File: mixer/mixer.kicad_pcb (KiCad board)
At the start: 2 copper layers, 20 parts, among them J1 in0, J2 in1, J3 in2, J4 out, J5 Conn_01x02, U1 OPA2134, U2 TLE2426xD

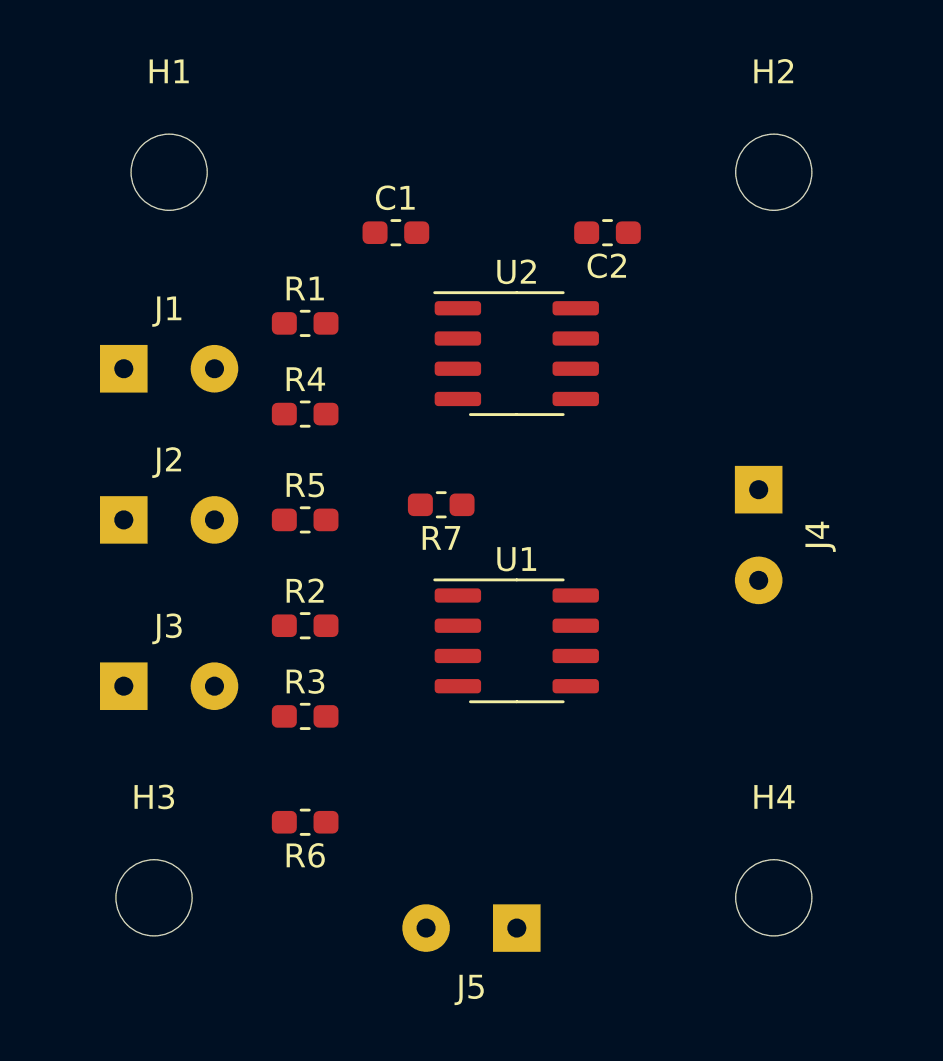
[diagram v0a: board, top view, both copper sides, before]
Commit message: Better placement
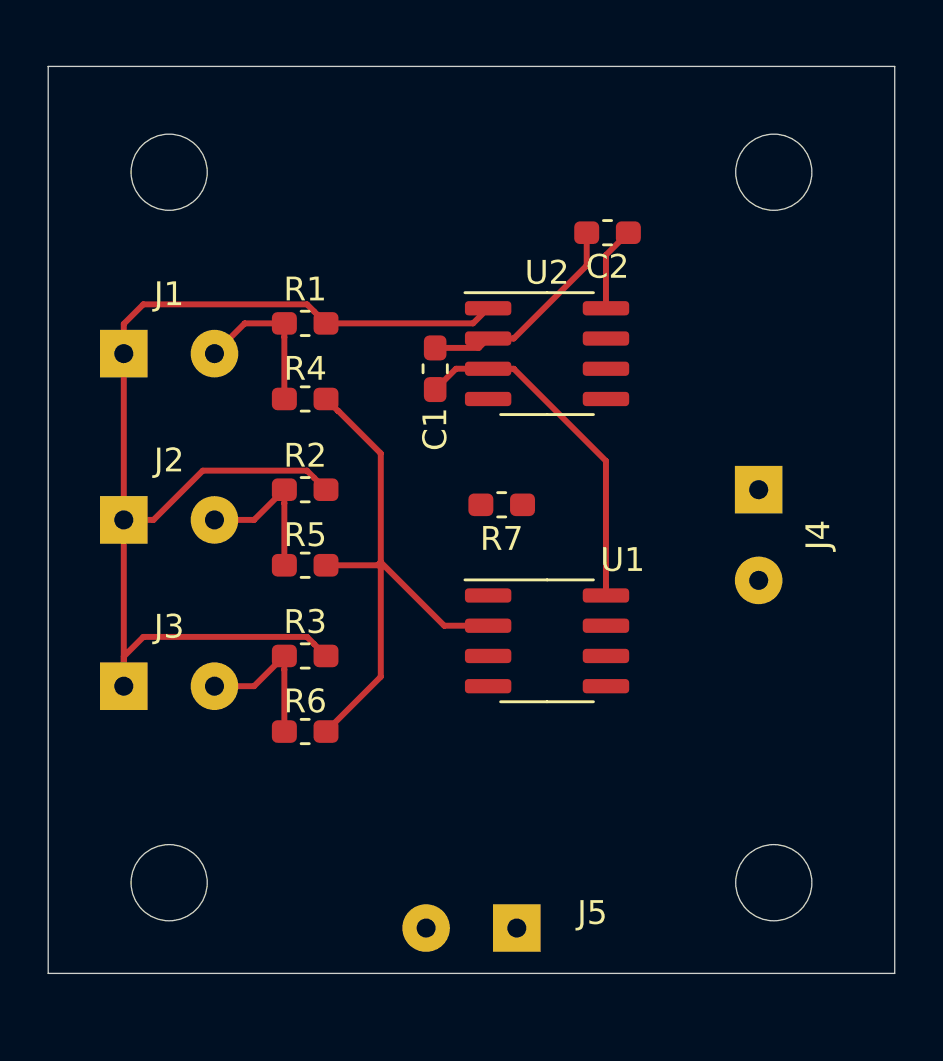
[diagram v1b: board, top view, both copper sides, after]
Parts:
- moved C1 5.95 mm to (148.3, 73.7), turned to 270 degrees
- moved R2 5.72 mm to (142.9, 78.7)
- moved R6 3.81 mm to (142.9, 88.9)
- moved R3 2.54 mm to (142.9, 85.7)
- moved R7 2.54 mm to (151.1, 79.4)
- moved R5 1.91 mm to (142.9, 81.9), turned to 180 degrees
- moved U1 1.27 mm to (153.0, 85.1)
- moved U2 1.27 mm to (153.0, 73.0)
- moved H3 0.90 mm to (137.2, 95.2)
- moved H4 0.64 mm to (162.6, 95.2)
- moved J1 0.63 mm to (135.3, 73.0)
- moved R4 0.63 mm to (142.9, 74.9), turned to 180 degrees
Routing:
- net GNDA: track 0.00 -> 51.6 mm
- net Net-(R4-Pad1): track 0.00 -> 23.9 mm
- net +9V: track 0.00 -> 14.8 mm
- net GND: track 0.00 -> 9.18 mm
- net Net-(J3-Pad2): track 0.00 -> 6.64 mm
- net Net-(J2-Pad2): track 0.00 -> 6.64 mm
- net Net-(J1-Pad2): track 0.00 -> 6.64 mm
- net Net-(C2-Pad1): track 0.00 -> 3.56 mm
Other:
- board outline added: 35.6 x 38.1 mm

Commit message: Routed
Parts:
- moved R7 0.92 mm to (150.9, 80.3)
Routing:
- net GND: track 9.18 -> 77.4 mm
- net +9V: track 14.8 -> 50.0 mm
- net GNDA: track 51.6 -> 84.9 mm
- net Net-(J4-Pad1): track 0.00 -> 16.0 mm
- net Net-(R4-Pad1): track 23.9 -> 29.3 mm
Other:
- board text added: "mixer v1"
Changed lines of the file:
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@@
   (general
     (thickness 1.6)
-    (drawings 4)
-    (tracks 54)
+    (drawings 5)
+    (tracks 89)
     (zones 0)
     (modules 20)
@@
   )
   (module Resistor_SMD:R_0603_1608Metric_Pad1.05x0.95mm_HandSolder (layer F.Cu)
-    (at 151.13 79.375 180)
+    (at 150.876 80.264 180)
     (descr "Resistor SMD 0603 (1608 Metric), square (rectangular) end terminal, IPC_7351 nominal with elongated pad for handsoldering. (Body size source: http://www.tortai-tech.com/upload/download/2011102023233369053.pdf), generated with kicad-footprint-generator")
     (tags "resistor handsolder")
@@
     )
   )
+  (gr_text "mixer v1" (at 149.098 63.246) (layer F.SilkS)
+    (effects (font (size 1.5 1.5) (thickness 0.3)))
+  )
   (gr_line (start 132.08 99.06) (end 132.08 60.96) (layer Edge.Cuts) (width 0.05))
   (gr_line (start 167.64 99.06) (end 132.08 99.06) (layer Edge.Cuts) (width 0.05))
@@
   (segment (start 149.211 73.66) (end 150.56 73.66) (width 0.25) (layer F.Cu) (net 1))
   (segment (start 148.336 74.535) (end 149.211 73.66) (width 0.25) (layer F.Cu) (net 1))
-  (segment (start 155.51 82.785) (end 155.51 83.185) (width 0.25) (layer F.Cu) (net 1))
-  (segment (start 155.51 77.535) (end 155.51 82.785) (width 0.25) (layer F.Cu) (net 1))
-  (segment (start 151.635 73.66) (end 155.51 77.535) (width 0.25) (layer F.Cu) (net 1))
+  (segment (start 151.765 95.90551) (end 151.765 97.155) (width 0.25) (layer F.Cu) (net 1))
+  (segment (start 163.249491 84.421019) (end 151.765 95.90551) (width 0.25) (layer F.Cu) (net 1))
+  (segment (start 155.390509 77.415509) (end 163.184491 77.415509) (width 0.25) (layer F.Cu) (net 1))
+  (segment (start 163.184491 77.415509) (end 163.249491 77.480509) (width 0.25) (layer F.Cu) (net 1))
+  (segment (start 151.635 73.66) (end 155.390509 77.415509) (width 0.25) (layer F.Cu) (net 1))
   (segment (start 150.56 73.66) (end 151.635 73.66) (width 0.25) (layer F.Cu) (net 1))
+  (segment (start 163.249491 80.953491) (end 157.741509 80.953491) (width 0.25) (layer F.Cu) (net 1))
+  (segment (start 157.741509 80.953491) (end 155.51 83.185) (width 0.25) (layer F.Cu) (net 1))
+  (segment (start 163.249491 77.480509) (end 163.249491 80.953491) (width 0.25) (layer F.Cu) (net 1))
+  (segment (start 163.249491 80.953491) (end 163.249491 84.421019) (width 0.25) (layer F.Cu) (net 1))
   (segment (start 154.7 69.325) (end 151.635 72.39) (width 0.25) (layer F.Cu) (net 2))
   (segment (start 151.635 72.39) (end 150.56 72.39) (width 0.25) (layer F.Cu) (net 2))
@@
   (segment (start 150.165 72.785) (end 150.56 72.39) (width 0.25) (layer F.Cu) (net 2))
   (segment (start 148.336 72.785) (end 150.165 72.785) (width 0.25) (layer F.Cu) (net 2))
+  (segment (start 150.56 94.55) (end 147.955 97.155) (width 0.25) (layer F.Cu) (net 2))
+  (segment (start 150.56 86.995) (end 150.56 94.55) (width 0.25) (layer F.Cu) (net 2))
+  (segment (start 137.751018 67.945) (end 133.35 72.346018) (width 0.25) (layer F.Cu) (net 2))
+  (segment (start 154.7 67.945) (end 137.751018 67.945) (width 0.25) (layer F.Cu) (net 2))
+  (segment (start 146.541508 97.155) (end 147.955 97.155) (width 0.25) (layer F.Cu) (net 2))
+  (segment (start 142.831018 97.155) (end 146.541508 97.155) (width 0.25) (layer F.Cu) (net 2))
+  (segment (start 133.35 87.673982) (end 142.831018 97.155) (width 0.25) (layer F.Cu) (net 2))
+  (segment (start 133.35 72.346018) (end 133.35 87.673982) (width 0.25) (layer F.Cu) (net 2))
   (segment (start 155.51 68.885) (end 156.45 67.945) (width 0.25) (layer F.Cu) (net 3))
   (segment (start 155.51 71.12) (end 155.51 68.885) (width 0.25) (layer F.Cu) (net 3))
@@
   (segment (start 149.925 71.755) (end 150.56 71.12) (width 0.25) (layer F.Cu) (net 4))
   (segment (start 143.75 71.755) (end 149.925 71.755) (width 0.25) (layer F.Cu) (net 4))
+  (segment (start 158.75 85.725) (end 161.925 82.55) (width 0.25) (layer F.Cu) (net 4))
+  (segment (start 155.51 85.725) (end 158.75 85.725) (width 0.25) (layer F.Cu) (net 4))
+  (segment (start 155.51 86.995) (end 155.51 85.725) (width 0.25) (layer F.Cu) (net 4))
+  (segment (start 151.635 85.725) (end 155.51 85.725) (width 0.25) (layer F.Cu) (net 4))
+  (segment (start 150.56 85.725) (end 151.635 85.725) (width 0.25) (layer F.Cu) (net 4))
+  (segment (start 135.255 88.24449) (end 137.43451 90.424) (width 0.25) (layer F.Cu) (net 4))
+  (segment (start 135.255 86.995) (end 135.255 88.24449) (width 0.25) (layer F.Cu) (net 4))
+  (segment (start 149.485 85.725) (end 150.56 85.725) (width 0.25) (layer F.Cu) (net 4))
+  (segment (start 144.786 90.424) (end 149.485 85.725) (width 0.25) (layer F.Cu) (net 4))
+  (segment (start 137.43451 90.424) (end 144.786 90.424) (width 0.25) (layer F.Cu) (net 4))
   (segment (start 140.335 71.755) (end 142 71.755) (width 0.25) (layer F.Cu) (net 5))
   (segment (start 139.065 73.025) (end 140.335 71.755) (width 0.25) (layer F.Cu) (net 5))
@@
   (segment (start 142 86.3) (end 142 88.9) (width 0.25) (layer F.Cu) (net 7))
   (segment (start 142 85.725) (end 142 86.3) (width 0.25) (layer F.Cu) (net 7))
+  (segment (start 150.754072 82.990928) (end 150.56 83.185) (width 0.25) (layer F.Cu) (net 8))
+  (segment (start 155.005 78.74) (end 161.925 78.74) (width 0.25) (layer F.Cu) (net 8))
+  (segment (start 150.56 80.823) (end 150.001 80.264) (width 0.25) (layer F.Cu) (net 8))
+  (segment (start 150.56 83.185) (end 150.56 80.823) (width 0.25) (layer F.Cu) (net 8))
+  (segment (start 151.525 78.74) (end 155.005 78.74) (width 0.25) (layer F.Cu) (net 8))
+  (segment (start 150.001 80.264) (end 151.525 78.74) (width 0.25) (layer F.Cu) (net 8))
   (segment (start 144.263072 75.429072) (end 146.05 77.216) (width 0.25) (layer F.Cu) (net 9))
   (segment (start 146.05 86.6) (end 143.75 88.9) (width 0.25) (layer F.Cu) (net 9))
@@
   (segment (start 148.717 84.455) (end 150.56 84.455) (width 0.25) (layer F.Cu) (net 9))
   (segment (start 146.05 81.788) (end 148.717 84.455) (width 0.25) (layer F.Cu) (net 9))
+  (segment (start 151.635 84.455) (end 150.56 84.455) (width 0.25) (layer F.Cu) (net 9))
+  (segment (start 151.86001 80.94801) (end 151.86001 84.22999) (width 0.25) (layer F.Cu) (net 9))
+  (segment (start 151.751 80.839) (end 151.86001 80.94801) (width 0.25) (layer F.Cu) (net 9))
+  (segment (start 151.86001 84.22999) (end 151.635 84.455) (width 0.25) (layer F.Cu) (net 9))
+  (segment (start 151.751 80.264) (end 151.751 80.839) (width 0.25) (layer F.Cu) (net 9))
 )

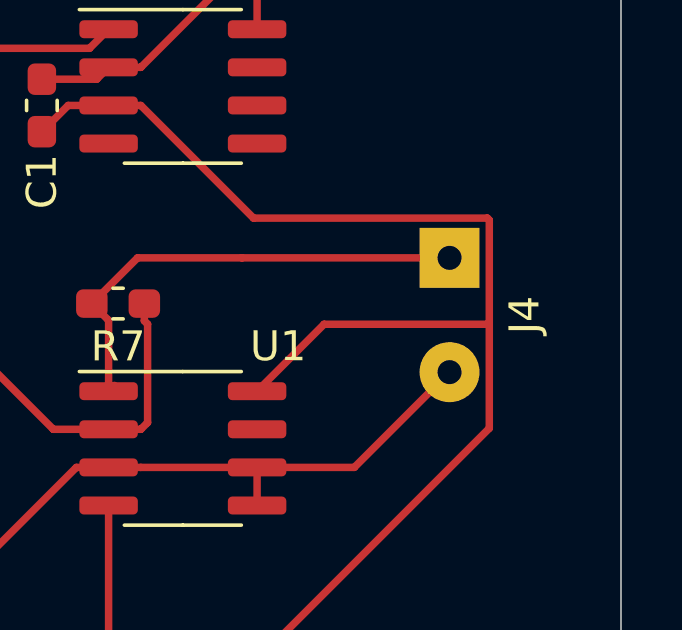
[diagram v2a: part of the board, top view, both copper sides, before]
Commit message: Use consistent GNDA pin
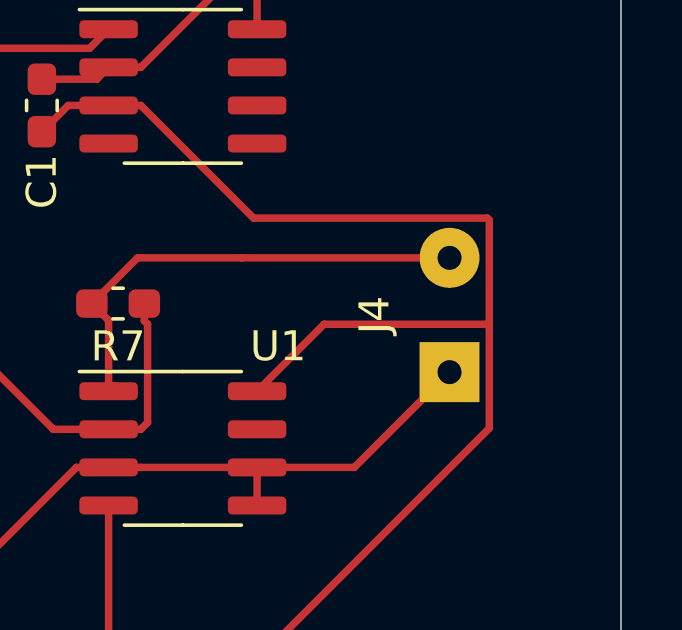
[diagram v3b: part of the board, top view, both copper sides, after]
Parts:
- moved J4 3.81 mm to (161.9, 82.5), turned to 90 degrees
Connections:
- J4 pad 1: Net-(J4-Pad1) -> GNDA
- J4 pad 2: GNDA -> Net-(J4-Pad2)
- R7 pad 2: Net-(J4-Pad1) -> Net-(J4-Pad2)
- U1 pad 1: Net-(J4-Pad1) -> Net-(J4-Pad2)
- U1 pad 7: Net-(U1-Pad7) -> (no net)
- U2 pad 4: Net-(U2-Pad4) -> (no net)
- U2 pad 5: Net-(U2-Pad5) -> (no net)
- U2 pad 6: Net-(U2-Pad6) -> (no net)
- U2 pad 7: Net-(U2-Pad7) -> (no net)
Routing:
- net Net-(J4-Pad2): track 0.00 -> 16.0 mm
- net Net-(J4-Pad1): track 16.0 -> 0.00 mm
